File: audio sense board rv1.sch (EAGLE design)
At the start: 33 parts, among them IC2 TSOP38238, J1 PJRAN1X1U01X, J2 PJRAN1X1U01X, Q1 2N3904, Q2 2N3904

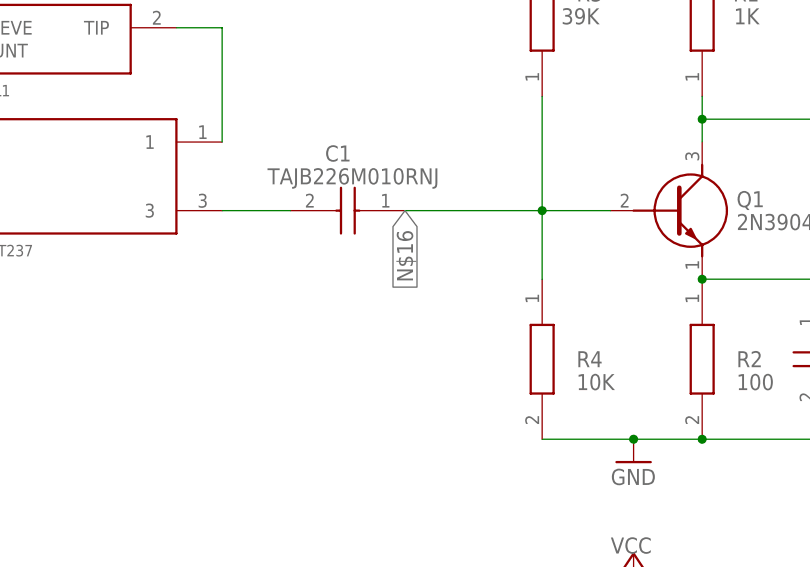
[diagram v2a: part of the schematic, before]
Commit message: update pad sizes
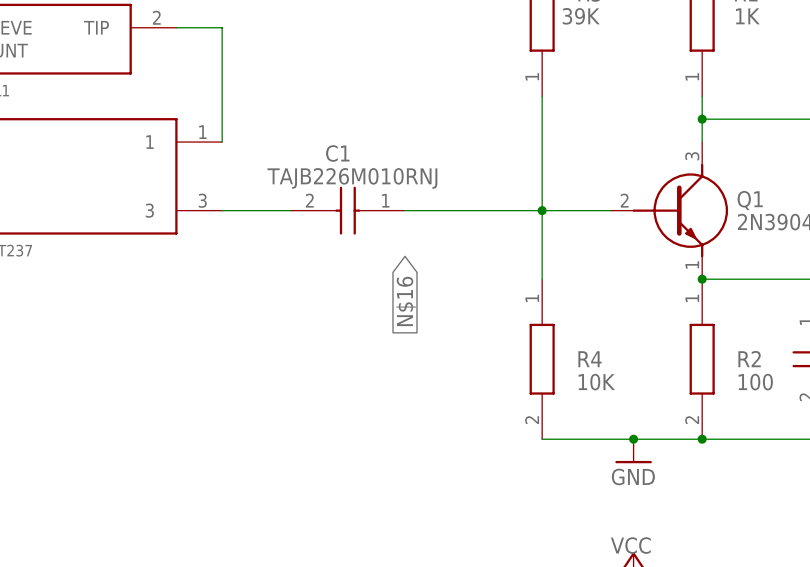
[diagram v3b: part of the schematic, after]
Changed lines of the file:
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@@
 <grid distance="0.1" unitdist="inch" unit="inch" style="lines" multiple="1" display="no" altdistance="0.01" altunitdist="inch" altunit="inch"/>
 <layers>
-<layer number="1" name="Top" color="4" fill="1" visible="yes" active="no"/>
-<layer number="16" name="Bottom" color="1" fill="1" visible="yes" active="no"/>
-<layer number="17" name="Pads" color="2" fill="1" visible="yes" active="no"/>
-<layer number="18" name="Vias" color="2" fill="1" visible="yes" active="no"/>
-<layer number="19" name="Unrouted" color="6" fill="1" visible="yes" active="no"/>
-<layer number="20" name="Dimension" color="24" fill="1" visible="yes" active="no"/>
-<layer number="21" name="tPlace" color="7" fill="1" visible="yes" active="no"/>
-<layer number="22" name="bPlace" color="7" fill="1" visible="yes" active="no"/>
-<layer number="23" name="tOrigins" color="15" fill="1" visible="yes" active="no"/>
-<layer number="24" name="bOrigins" color="15" fill="1" visible="yes" active="no"/>
-<layer number="25" name="tNames" color="7" fill="1" visible="yes" active="no"/>
-<layer number="26" name="bNames" color="7" fill="1" visible="yes" active="no"/>
-<layer number="27" name="tValues" color="7" fill="1" visible="yes" active="no"/>
-<layer number="28" name="bValues" color="7" fill="1" visible="yes" active="no"/>
+<layer number="1" name="Top" color="4" fill="1" visible="no" active="no"/>
+<layer number="16" name="Bottom" color="1" fill="1" visible="no" active="no"/>
+<layer number="17" name="Pads" color="2" fill="1" visible="no" active="no"/>
+<layer number="18" name="Vias" color="2" fill="1" visible="no" active="no"/>
+<layer number="19" name="Unrouted" color="6" fill="1" visible="no" active="no"/>
+<layer number="20" name="Dimension" color="24" fill="1" visible="no" active="no"/>
+<layer number="21" name="tPlace" color="7" fill="1" visible="no" active="no"/>
+<layer number="22" name="bPlace" color="7" fill="1" visible="no" active="no"/>
+<layer number="23" name="tOrigins" color="15" fill="1" visible="no" active="no"/>
+<layer number="24" name="bOrigins" color="15" fill="1" visible="no" active="no"/>
+<layer number="25" name="tNames" color="7" fill="1" visible="no" active="no"/>
+<layer number="26" name="bNames" color="7" fill="1" visible="no" active="no"/>
+<layer number="27" name="tValues" color="7" fill="1" visible="no" active="no"/>
+<layer number="28" name="bValues" color="7" fill="1" visible="no" active="no"/>
 <layer number="29" name="tStop" color="7" fill="3" visible="no" active="no"/>
 <layer number="30" name="bStop" color="7" fill="6" visible="no" active="no"/>
@@
 <layer number="35" name="tGlue" color="7" fill="4" visible="no" active="no"/>
 <layer number="36" name="bGlue" color="7" fill="5" visible="no" active="no"/>
-<layer number="37" name="tTest" color="7" fill="1" visible="yes" active="no"/>
-<layer number="38" name="bTest" color="7" fill="1" visible="yes" active="no"/>
+<layer number="37" name="tTest" color="7" fill="1" visible="no" active="no"/>
+<layer number="38" name="bTest" color="7" fill="1" visible="no" active="no"/>
 <layer number="39" name="tKeepout" color="4" fill="11" visible="no" active="no"/>
 <layer number="40" name="bKeepout" color="1" fill="11" visible="no" active="no"/>
@@
 <layer number="44" name="Drills" color="7" fill="1" visible="no" active="no"/>
 <layer number="45" name="Holes" color="7" fill="1" visible="no" active="no"/>
-<layer number="46" name="Milling" color="3" fill="1" visible="yes" active="no"/>
-<layer number="47" name="Measures" color="7" fill="1" visible="yes" active="no"/>
-<layer number="48" name="Document" color="7" fill="1" visible="yes" active="no"/>
-<layer number="49" name="Reference" color="7" fill="1" visible="yes" active="no"/>
-<layer number="50" name="dxf" color="7" fill="1" visible="yes" active="no"/>
-<layer number="51" name="tDocu" color="7" fill="1" visible="yes" active="no"/>
-<layer number="52" name="bDocu" color="7" fill="1" visible="yes" active="no"/>
-<layer number="53" name="tGND_GNDA" color="7" fill="9" visible="yes" active="no"/>
-<layer number="54" name="bGND_GNDA" color="1" fill="9" visible="yes" active="no"/>
-<layer number="56" name="wert" color="7" fill="1" visible="yes" active="no"/>
-<layer number="57" name="tCAD" color="7" fill="1" visible="yes" active="no"/>
-<layer number="59" name="tCarbon" color="7" fill="1" visible="yes" active="no"/>
-<layer number="60" name="bCarbon" color="7" fill="1" visible="yes" active="no"/>
+<layer number="46" name="Milling" color="3" fill="1" visible="no" active="no"/>
+<layer number="47" name="Measures" color="7" fill="1" visible="no" active="no"/>
+<layer number="48" name="Document" color="7" fill="1" visible="no" active="no"/>
+<layer number="49" name="Reference" color="7" fill="1" visible="no" active="no"/>
+<layer number="50" name="dxf" color="7" fill="1" visible="no" active="no"/>
+<layer number="51" name="tDocu" color="7" fill="1" visible="no" active="no"/>
+<layer number="52" name="bDocu" color="7" fill="1" visible="no" active="no"/>
+<layer number="53" name="tGND_GNDA" color="7" fill="9" visible="no" active="no"/>
+<layer number="54" name="bGND_GNDA" color="1" fill="9" visible="no" active="no"/>
+<layer number="56" name="wert" color="7" fill="1" visible="no" active="no"/>
+<layer number="57" name="tCAD" color="7" fill="1" visible="no" active="no"/>
+<layer number="59" name="tCarbon" color="7" fill="1" visible="no" active="no"/>
+<layer number="60" name="bCarbon" color="7" fill="1" visible="no" active="no"/>
 <layer number="88" name="SimResults" color="9" fill="1" visible="yes" active="yes"/>
 <layer number="89" name="SimProbes" color="9" fill="1" visible="yes" active="yes"/>
@@
 <pinref part="R4" gate="G$1" pin="1"/>
 <wire x1="0" y1="50.8" x2="0" y2="58.42" width="0.1524" layer="91"/>
-<label x="-15.24" y="58.42" size="1.778" layer="95" rot="R270" xref="yes"/>
-</segment>
-</net>
+<label x="-15.24" y="53.34" size="1.778" layer="95" rot="R270" xref="yes"/>
+</segment>
+</net>

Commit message: update pads R14
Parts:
- R14: device Samac Populated:CRCW1206100RJNEAC -> Samac Populated:ERJ8GEYJ101V
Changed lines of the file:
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@@
 <part name="R13" library="Samac Populated" deviceset="ERJ8GEYJ101V" device="" value="100"/>
 <part name="GND4" library="supply1" library_urn="urn:adsk.eagle:library:371" deviceset="GND" device=""/>
-<part name="R14" library="Samac Populated" deviceset="CRCW1206100RJNEAC" device="" value="100"/>
+<part name="R14" library="Samac Populated" deviceset="ERJ8GEYJ101V" device="" value="100"/>
 <part name="J1" library="Samac Populated" deviceset="PJRAN1X1U01X" device=""/>
 <part name="L1" library="My Library" deviceset="IT237" device="" value="IT237"/>
@@
 <pinref part="IR_LED" gate="G$1" pin="1"/>
 <wire x1="-142.24" y1="73.66" x2="-157.48" y2="73.66" width="0.1524" layer="91"/>
-<label x="-142.24" y="73.66" size="1.778" layer="95" rot="R180" xref="yes"/>
-</segment>
-</net>
+</segment>
+</net>
